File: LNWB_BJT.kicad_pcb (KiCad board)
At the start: 2 copper layers, 107 parts, among them J1 Input, J2 wire2board, J3 Input, J4 wire2board, Q1 2N4401, Q2 2N4401, Q3 2N3906, Q4 BD679, Q5 BD680, U1 TL072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

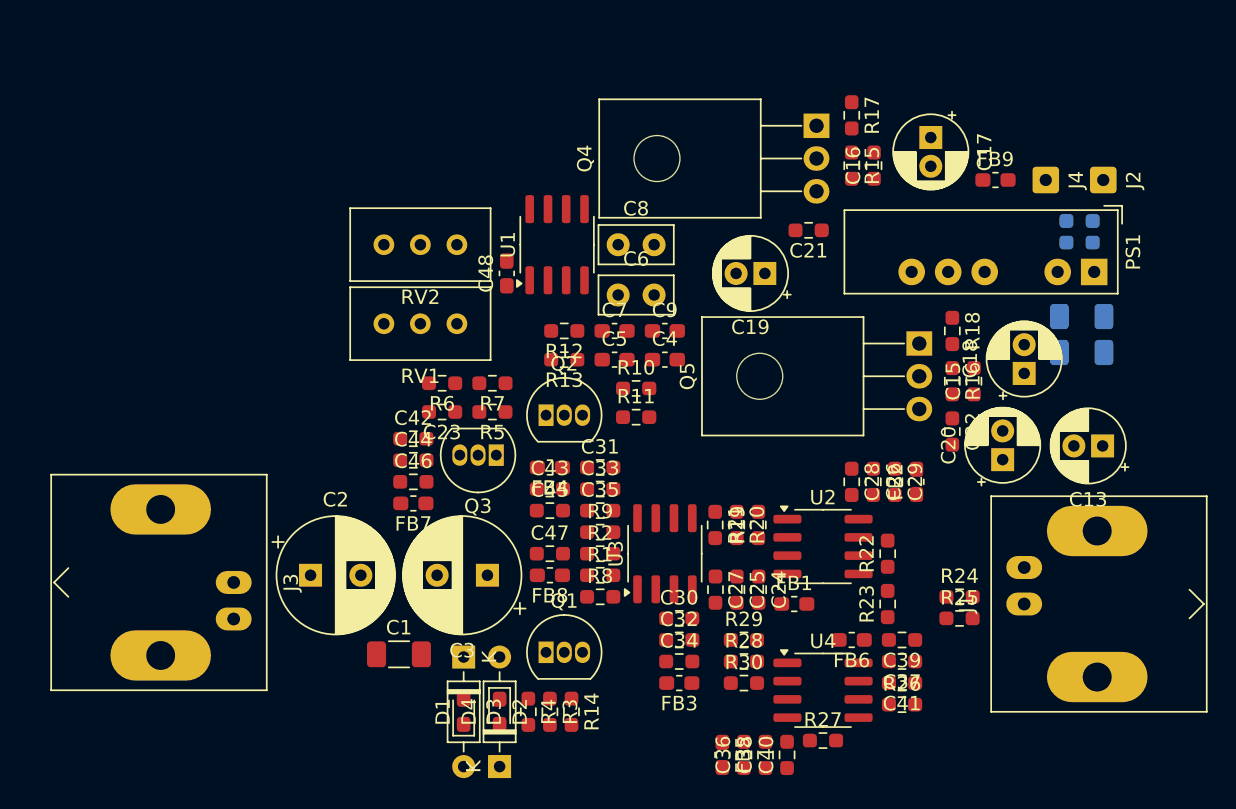
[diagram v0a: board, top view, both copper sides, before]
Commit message: Mounting holes, edge cuts.
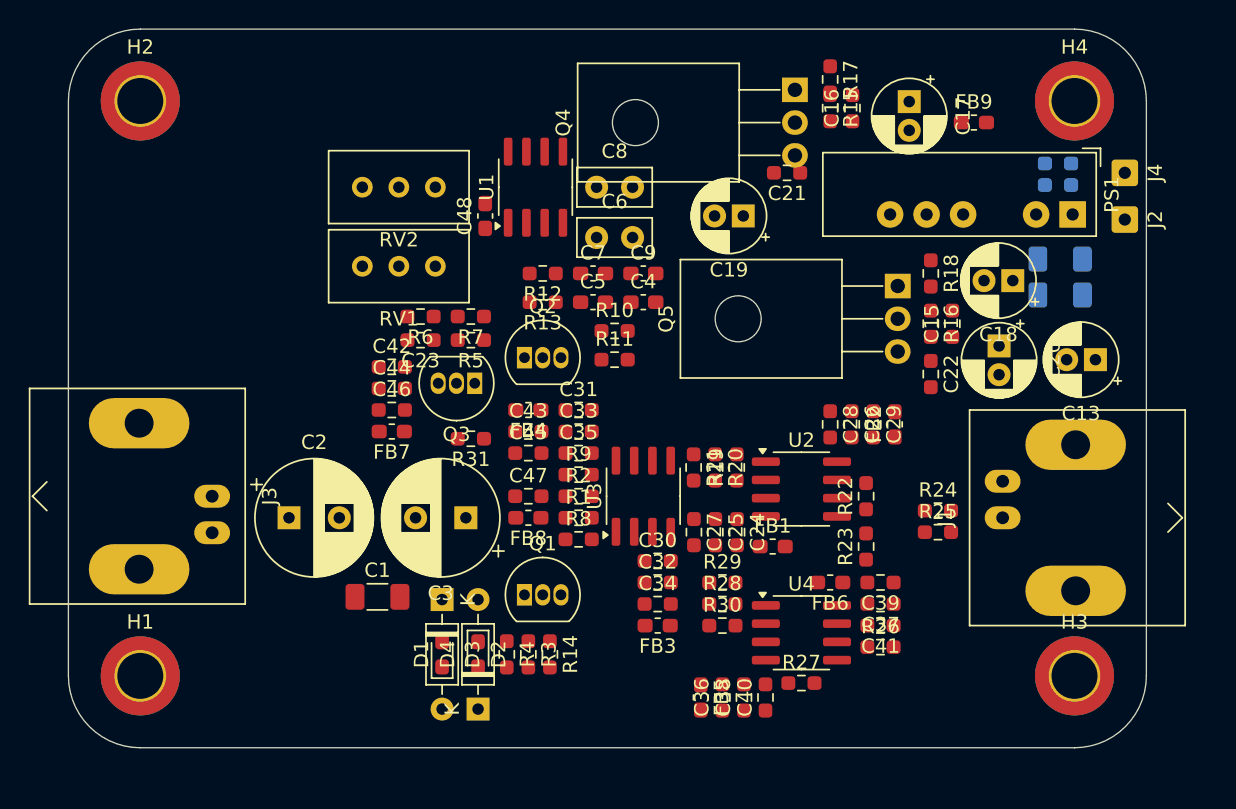
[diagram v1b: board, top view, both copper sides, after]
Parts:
- added H1: MountingHole, MountingHole:MountingHole_3.2mm_M3_ISO14580_Pad_TopBottom, F.Cu at (55.0, 120.0)
- added H2: MountingHole, MountingHole:MountingHole_3.2mm_M3_ISO14580_Pad_TopBottom, F.Cu at (55.0, 80.0)
- added H3: MountingHole, MountingHole:MountingHole_3.2mm_M3_ISO14580_Pad_TopBottom, F.Cu at (120.0, 120.0)
- added H4: MountingHole, MountingHole:MountingHole_3.2mm_M3_ISO14580_Pad_TopBottom, F.Cu at (120.0, 80.0)
- added R31: 1k, Resistor_SMD:R_0603_1608Metric_Pad0.98x0.95mm_HandSolder, F.Cu at (78.0, 103.5)
- moved C20 7.91 mm to (114.8, 97.0), turned to -90 degrees
- moved C18 6.50 mm to (115.7, 92.5), turned to 180 degrees
- moved J1 6.18 mm to (115.0, 109.0)
- moved J3 6.18 mm to (60.0, 107.5)
- moved R24 6.18 mm to (110.5, 108.5)
- moved R25 6.18 mm to (110.5, 110.0)
- moved C13 6.02 mm to (121.5, 98.0)
- moved J4 5.52 mm to (123.5, 85.0)
- moved C23 5.22 mm to (74.5, 96.6)
- moved C42 5.22 mm to (72.5, 98.5)
- moved C44 5.22 mm to (72.5, 100.0)
- moved C46 5.22 mm to (72.5, 101.5)
- moved FB7 5.22 mm to (72.5, 103.0)
- moved Q3 5.22 mm to (78.3, 99.6)
- moved R5 5.22 mm to (78.0, 96.6)
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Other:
- board outline added: 75 x 50 mm

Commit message: klfdsa.wq
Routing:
- net Net-(D1-A): track 0.00 -> 26.7 mm
- net Net-(J3-In): track 0.00 -> 13.4 mm
- net Net-(Q1-C): track 0.00 -> 6.70 mm
- net (no net): vias 0 -> 1
- added copper zone on In1.Cu, net GND
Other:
- copper layers 2 -> 4
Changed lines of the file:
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@@
 	(layers
 		(0 "F.Cu" signal)
+		(1 "In1.Cu" signal)
+		(2 "In2.Cu" signal)
 		(31 "B.Cu" signal)
 		(32 "B.Adhes" user "B.Adhesive")
@@
 	)
 	(setup
+		(stackup
+			(layer "F.SilkS"
+				(type "Top Silk Screen")
+			)
+			(layer "F.Paste"
+				(type "Top Solder Paste")
+			)
+			(layer "F.Mask"
+				(type "Top Solder Mask")
+				(thickness 0.01)
+			)
+			(layer "F.Cu"
+				(type "copper")
+				(thickness 0.035)
+			)
+			(layer "dielectric 1"
+				(type "prepreg")
+				(thickness 0.1)
+				(material "FR4")
+				(epsilon_r 4.5)
+				(loss_tangent 0.02)
+			)
+			(layer "In1.Cu"
+				(type "copper")
+				(thickness 0.035)
+			)
+			(layer "dielectric 2"
+				(type "core")
+				(thickness 1.24)
+				(material "FR4")
+				(epsilon_r 4.5)
+				(loss_tangent 0.02)
+			)
+			(layer "In2.Cu"
+				(type "copper")
+				(thickness 0.035)
+			)
+			(layer "dielectric 3"
+				(type "prepreg")
+				(thickness 0.1)
+				(material "FR4")
+				(epsilon_r 4.5)
+				(loss_tangent 0.02)
+			)
+			(layer "B.Cu"
+				(type "copper")
+				(thickness 0.035)
+			)
+			(layer "B.Mask"
+				(type "Bottom Solder Mask")
+				(thickness 0.01)
+			)
+			(layer "B.Paste"
+				(type "Bottom Solder Paste")
+			)
+			(layer "B.SilkS"
+				(type "Bottom Silk Screen")
+			)
+			(copper_finish "None")
+			(dielectric_constraints no)
+		)
 		(pad_to_mask_clearance 0)
 		(allow_soldermask_bridges_in_footprints no)
@@
 		(tags "CP Radial series Radial pin pitch 2.00mm  diameter 5mm Electrolytic Capacitor")
 		(property "Reference" "C18"
-			(at 1 -3.75 360)
+			(at 1 -3.75 0)
 			(layer "F.SilkS")
 			(effects
@@
 		)
 		(property "Value" "47u"
-			(at 1 3.75 360)
+			(at 1 3.75 0)
 			(layer "F.Fab")
 			(effects
@@
 		)
 		(fp_text user "${REFERENCE}"
-			(at 1 0 360)
+			(at 1 0 0)
 			(layer "F.Fab")
 			(effects
@@
 		(layer "Edge.Cuts")
 	)
+	(via
+		(at 83.4 120.6)
+		(size 0.6)
+		(drill 0.3)
+		(layers "F.Cu" "B.Cu")
+		(net 0)
+	)
+	(segment
+		(start 60 107.5)
+		(end 63.847349 107.5)
+		(width 1)
+		(layer "F.Cu")
+		(net 1)
+	)
+	(segment
+		(start 65.347349 109)
+		(end 65.347349 109.909849)
+		(width 1)
+		(layer "F.Cu")
+		(net 1)
+	)
+	(segment
+		(start 63.847349 107.5)
+		(end 65.347349 109)
+		(width 1)
+		(layer "F.Cu")
+		(net 1)
+	)
+	(segment
+		(start 65.347349 109.909849)
+		(end 69.9375 114.5)
+		(width 1)
+		(layer "F.Cu")
+		(net 1)
+	)
+	(segment
+		(start 83 117.625)
+		(end 83 114.36)
+		(width 1)
+		(layer "F.Cu")
+		(net 2)
+	)
+	(segment
+		(start 76 117.625)
+		(end 76 114.69)
+		(width 1)
+		(layer "F.Cu")
+		(net 2)
+	)
+	(segment
+		(start 73.0625 114.5)
+		(end 78.31 114.5)
+		(width 1)
+		(layer "F.Cu")
+		(net 2)
+	)
+	(segment
+		(start 82 117.5875)
+		(end 82.0375 117.625)
+		(width 1)
+		(layer "F.Cu")
+		(net 2)
+	)
+	(segment
+		(start 82.0375 117.625)
+		(end 83 117.625)
+		(width 1)
+		(layer "F.Cu")
+		(net 2)
+	)
+	(segment
+		(start 78.5 117.625)
+		(end 83.4625 117.625)
+		(width 1)
+		(layer "F.Cu")
+		(net 2)
+	)
+	(segment
+		(start 83.4625 117.625)
+		(end 83.5 117.5875)
+		(width 1)
+		(layer "F.Cu")
+		(net 2)
+	)
+	(segment
+		(start 78.5 117.625)
+		(end 78.5 114.69)
+		(width 1)
+		(layer "F.Cu")
+		(net 2)
+	)
+	(segment
+		(start 78.5 109.847349)
+		(end 77.652651 109)
+		(width 1)
+		(layer "F.Cu")
+		(net 2)
+	)
+	(segment
+		(start 78.31 114.5)
+		(end 78.5 114.69)
+		(width 1)
+		(layer "F.Cu")
+		(net 2)
+	)
+	(segment
+		(start 78.5 114.69)
+		(end 78.5 109.847349)
+		(width 1)
+		(layer "F.Cu")
+		(net 2)
+	)
+	(segment
+		(start 86.4125 110.5)
+		(end 86.4125 109)
+		(width 1)
+		(layer "F.Cu")
+		(net 30)
+	)
+	(segment
+		(start 86.4125 112.9875)
+		(end 86.4125 110.5)
+		(width 1)
+		(layer "F.Cu")
+		(net 30)
+	)
+	(segment
+		(start 84.27 114.36)
+		(end 85.04 114.36)
+		(width 1)
+		(layer "F.Cu")
+		(net 30)
+	)
+	(segment
+		(start 85.04 114.36)
+		(end 86.4125 112.9875)
+		(width 1)
+		(layer "F.Cu")
+		(net 30)
+	)
+	(zone
+		(net 28)
+		(net_name "GND")
+		(layer "In1.Cu")
+		(hatch edge 0.5)
+		(connect_pads
+			(clearance 0.5)
+		)
+		(min_thickness 0.25)
+		(filled_areas_thickness no)
+		(fill yes
+			(thermal_gap 0.5)
+			(thermal_bridge_width 0.5)
+		)
+		(polygon
+			(pts
+				(xy 50 75) (xy 125 75) (xy 125 125) (xy 50 125)
+			)
+		)
+	)
 )
